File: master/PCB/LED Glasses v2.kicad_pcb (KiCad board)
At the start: 2 copper layers, 85 parts, among them J1 Conn_01x01_Male, J2 Conn_01x01_Male, J3 Conn_01x01_Male, J4 Conn_01x01_Male, J5 Conn_01x01_Male

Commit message: test commit
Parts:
- moved J5 1.60 mm to (236.9, 101.0)
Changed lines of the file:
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@@
   )
   (module Connector_PinHeader_1.00mm:PinHeader_1x01_P1.00mm_Vertical_SMD_CUSTOM (layer F.Cu)
-    (at 236.730209 102.60337)
+    (at 236.8931 101.0158)
     (descr "surface-mounted straight pin header, 1x03, 1.00mm pitch, single row, style 1 (pin 1 left)")
     (tags "Surface mounted pin header SMD 1x03 1.00mm single row style1 pin1 left")

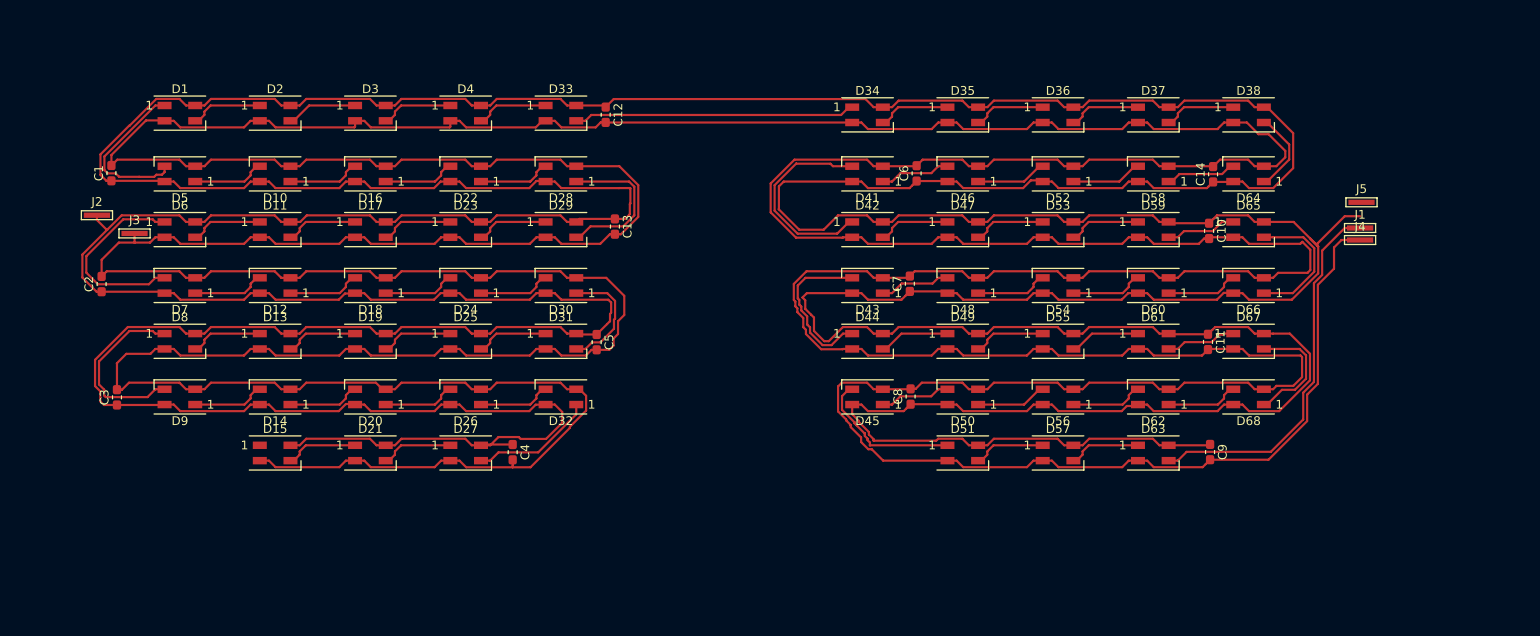
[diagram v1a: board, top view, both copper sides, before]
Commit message: PCB
Moved cutout to the appropriate layer
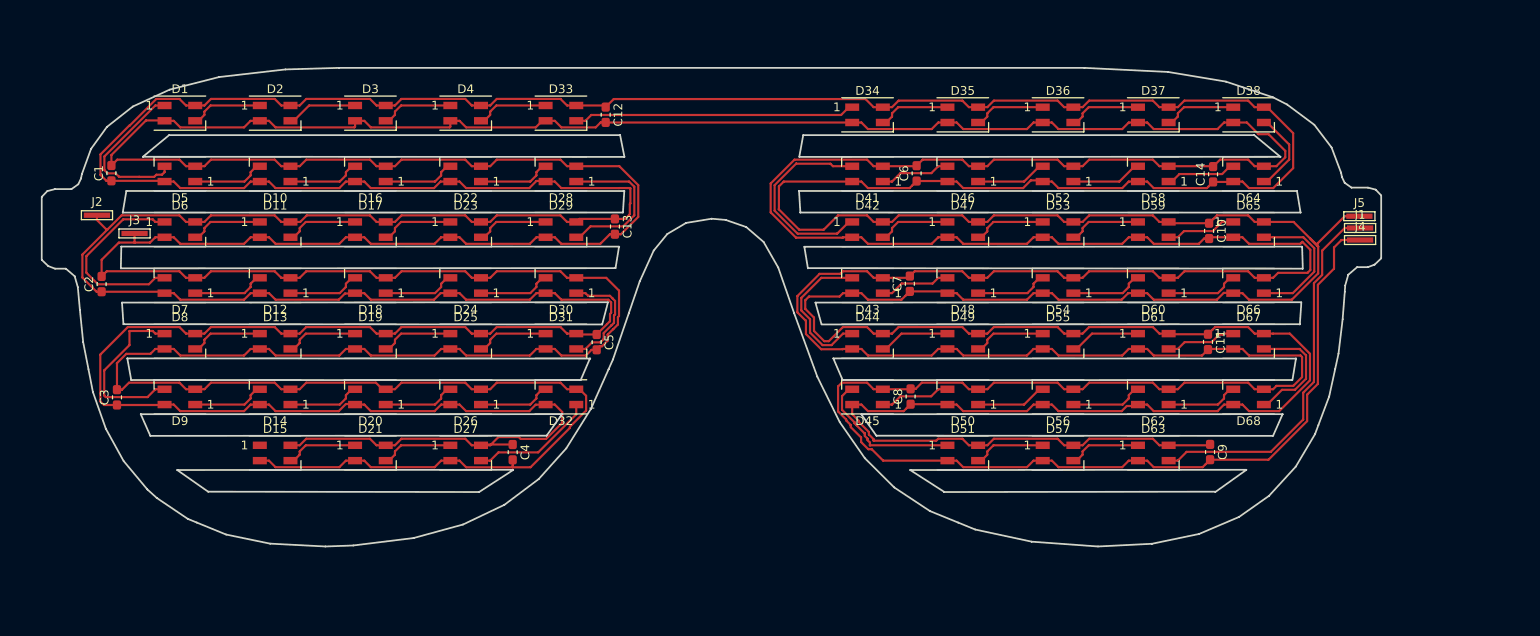
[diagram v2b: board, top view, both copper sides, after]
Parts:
- moved J5 1.61 mm to (236.7, 102.6)
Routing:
- net Net-(C1-Pad2): track 928.0 -> 925.5 mm
- net Net-(D43-Pad3): track 18.5 -> 17.1 mm
- net Net-(C1-Pad1): track 898.7 -> 897.5 mm
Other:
- board outline added: 152.9 x 54.6 mm

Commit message: Update LED Glasses v2.kicad_pcb
Updated PCB design files to use power and ground planes rather than traced connections
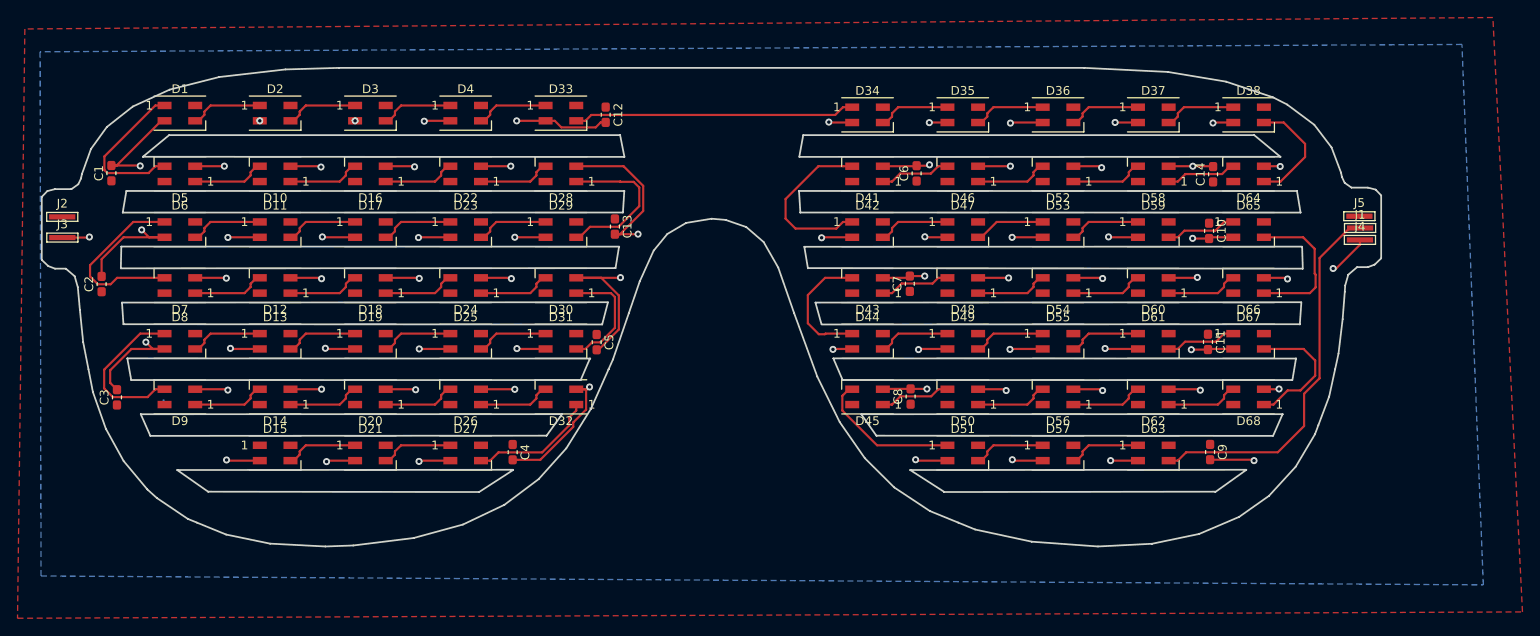
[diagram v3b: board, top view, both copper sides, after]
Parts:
- moved J3 8.26 mm to (88.6, 105.0)
- moved J2 3.97 mm to (88.6, 102.7)
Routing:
- net Net-(C1-Pad1): track 897.5 -> 0.00 mm
- net Net-(C1-Pad2): track 925.5 -> 311.4 mm, vias 0 -> 69
- net Net-(D41-Pad3): track 23.4 -> 19.8 mm
- net Net-(D38-Pad3): track 9.58 -> 13.1 mm
- net Net-(D43-Pad3): track 17.1 -> 14.7 mm
- net Net-(D8-Pad1): track 20.0 -> 18.4 mm
- net Net-(D67-Pad3): track 13.8 -> 15.4 mm
- net Net-(D6-Pad1): track 22.5 -> 21.0 mm
- net Net-(D65-Pad3): track 15.7 -> 17.0 mm
- net Net-(D1-Pad1): track 19.3 -> 18.2 mm
- net Net-(D45-Pad3): track 17.3 -> 16.8 mm
- net (no net): track 0.00 -> 0.55 mm
- added copper zone on F.Cu, net Net-(C1-Pad1)
- added copper zone on B.Cu, net Net-(C1-Pad2)

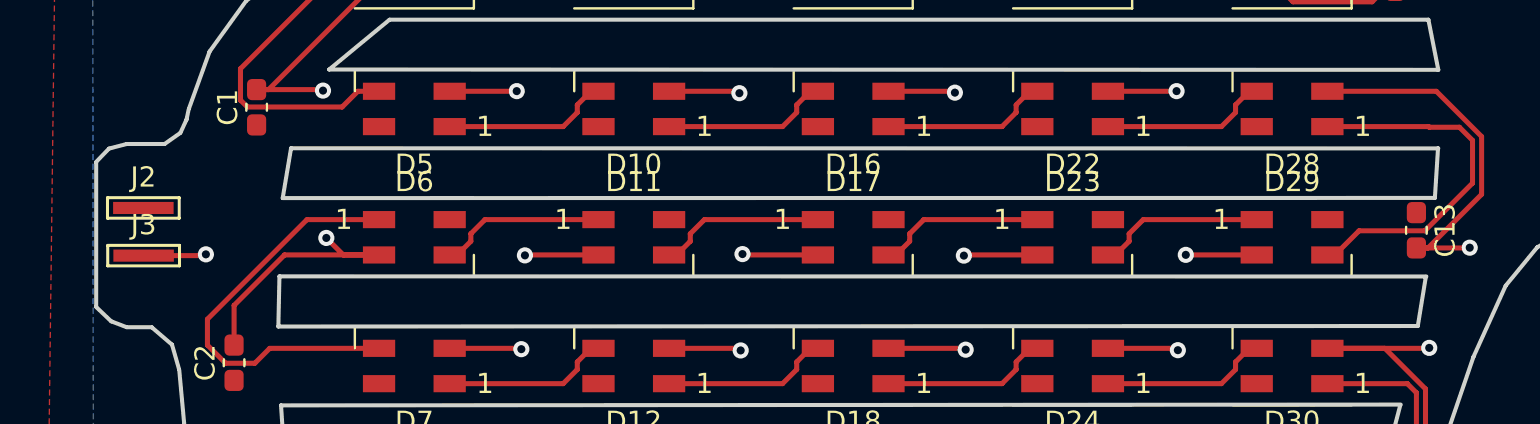
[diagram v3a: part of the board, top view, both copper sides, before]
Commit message: Moved left breakout pads
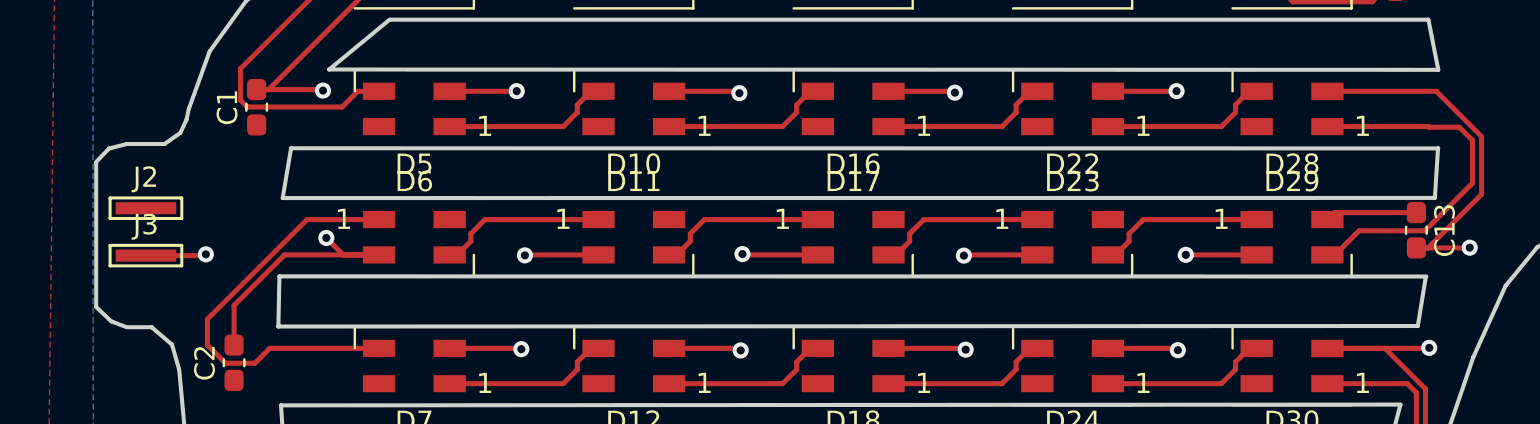
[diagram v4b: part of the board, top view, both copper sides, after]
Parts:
- moved J2 0.13 mm to (88.7, 102.7)
- moved J3 0.11 mm to (88.7, 105.0)
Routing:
- net Net-(C1-Pad1): track 0.00 -> 4.56 mm
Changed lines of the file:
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@@
     (thickness 1.6)
     (drawings 156)
-    (tracks 606)
+    (tracks 608)
     (zones 0)
     (modules 85)
@@
   )
   (module Connector_PinHeader_1.00mm:PinHeader_1x01_P1.00mm_Vertical_SMD_CUSTOM (layer F.Cu)
-    (at 88.5698 102.6795)
+    (at 88.6968 102.6922)
     (descr "surface-mounted straight pin header, 1x03, 1.00mm pitch, single row, style 1 (pin 1 left)")
     (tags "Surface mounted pin header SMD 1x03 1.00mm single row style1 pin1 left")
@@
   )
   (module Connector_PinHeader_1.00mm:PinHeader_1x01_P1.00mm_Vertical_SMD_CUSTOM (layer F.Cu)
-    (at 88.5825 105.0417)
+    (at 88.6968 105.0417)
     (descr "surface-mounted straight pin header, 1x03, 1.00mm pitch, single row, style 1 (pin 1 left)")
     (tags "Surface mounted pin header SMD 1x03 1.00mm single row style1 pin1 left")
@@
   (segment (start 221.2 101.225) (end 220.20229 102.22271) (width 0.25) (layer F.Cu) (net 1))
   (segment (start 222.25 101.225) (end 221.2 101.225) (width 0.25) (layer F.Cu) (net 1))
+  (segment (start 147.5963 100.8787) (end 147.25 101.225) (width 0.25) (layer F.Cu) (net 2))
+  (segment (start 151.6634 100.8787) (end 147.5963 100.8787) (width 0.25) (layer F.Cu) (net 2))
   (segment (start 219.4394 115.725) (end 219.3671 115.7973) (width 0.25) (layer F.Cu) (net 3))
   (segment (start 222.25 115.725) (end 219.4394 115.725) (width 0.25) (layer F.Cu) (net 3))

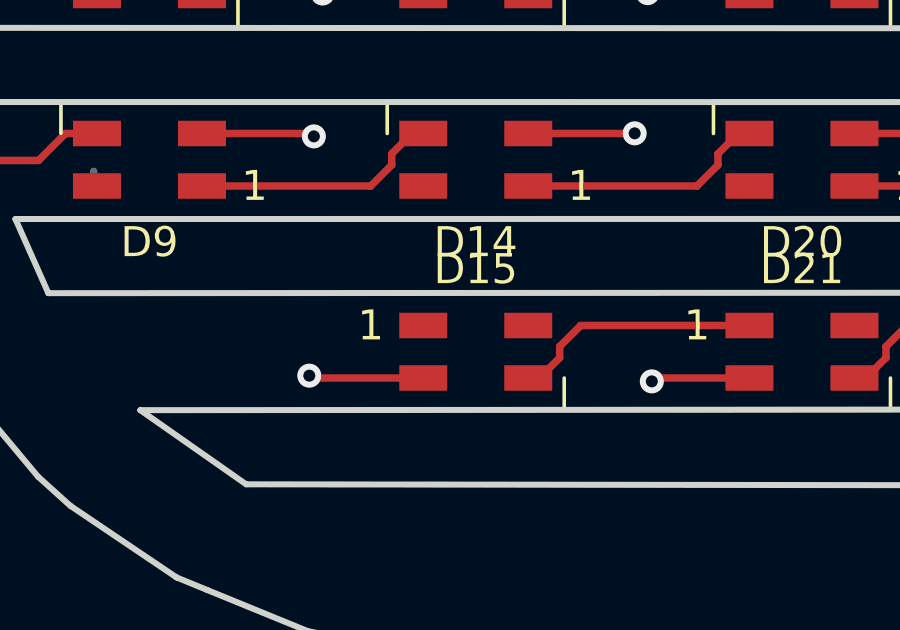
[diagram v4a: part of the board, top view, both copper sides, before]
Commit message: Moved left breakout pads x2
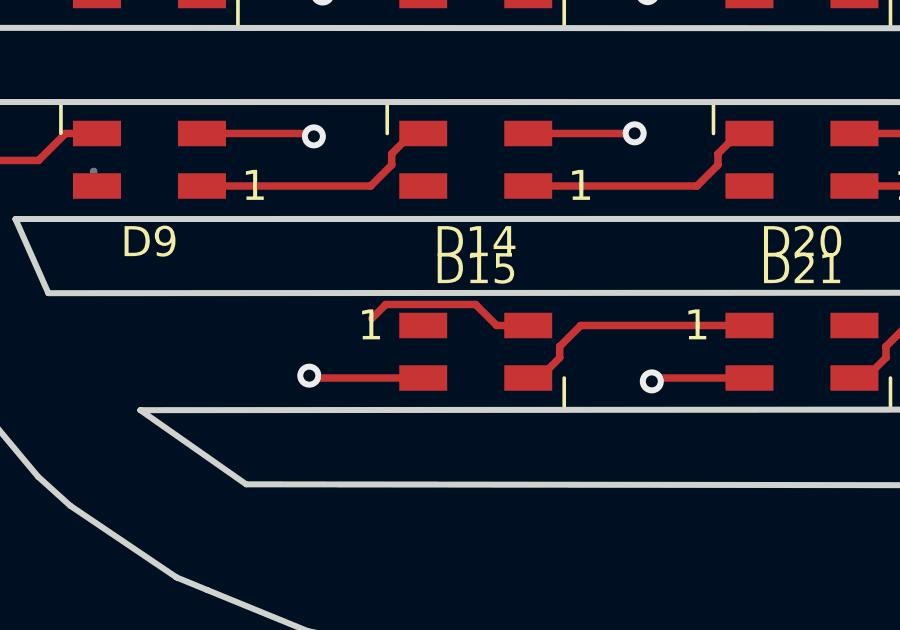
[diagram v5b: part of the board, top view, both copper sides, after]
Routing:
- net Net-(C1-Pad1): track 4.56 -> 10.3 mm
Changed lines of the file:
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@@
     (thickness 1.6)
     (drawings 156)
-    (tracks 608)
+    (tracks 612)
     (zones 0)
     (modules 85)
@@
   (segment (start 147.5963 100.8787) (end 147.25 101.225) (width 0.25) (layer F.Cu) (net 2))
   (segment (start 151.6634 100.8787) (end 147.5963 100.8787) (width 0.25) (layer F.Cu) (net 2))
+  (segment (start 112.874999 126.024999) (end 109.877501 126.024999) (width 0.25) (layer F.Cu) (net 2))
+  (segment (start 114.625 126.725) (end 113.575 126.725) (width 0.25) (layer F.Cu) (net 2))
+  (segment (start 113.575 126.725) (end 112.874999 126.024999) (width 0.25) (layer F.Cu) (net 2))
+  (segment (start 109.877501 126.024999) (end 109.4105 126.492) (width 0.25) (layer F.Cu) (net 2))
   (segment (start 219.4394 115.725) (end 219.3671 115.7973) (width 0.25) (layer F.Cu) (net 3))
   (segment (start 222.25 115.725) (end 219.4394 115.725) (width 0.25) (layer F.Cu) (net 3))

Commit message: gerber zip
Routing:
- net Net-(C1-Pad1): track 10.3 -> 924.1 mm
- net Net-(D41-Pad3): track 19.8 -> 23.1 mm
- net Net-(D65-Pad3): track 17.0 -> 15.8 mm
- removed copper zone on F.Cu, net Net-(C1-Pad1)
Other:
- net class Default: clearance 0.2 -> 0.125
- rule trace_clearance: 0.2 -> 0.125
